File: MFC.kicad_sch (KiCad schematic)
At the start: 29 parts, among them J1 DA15_Receptacle_MountingHoles, J12 Conn_01x01_Pin, J2 Conn_01x04_Pin, J4 647676-3, J5 Conn_01x03_Pin, J6 Conn_01x03_Pin, J7 Conn_01x02_Pin, J8 Conn_01x03_Socket

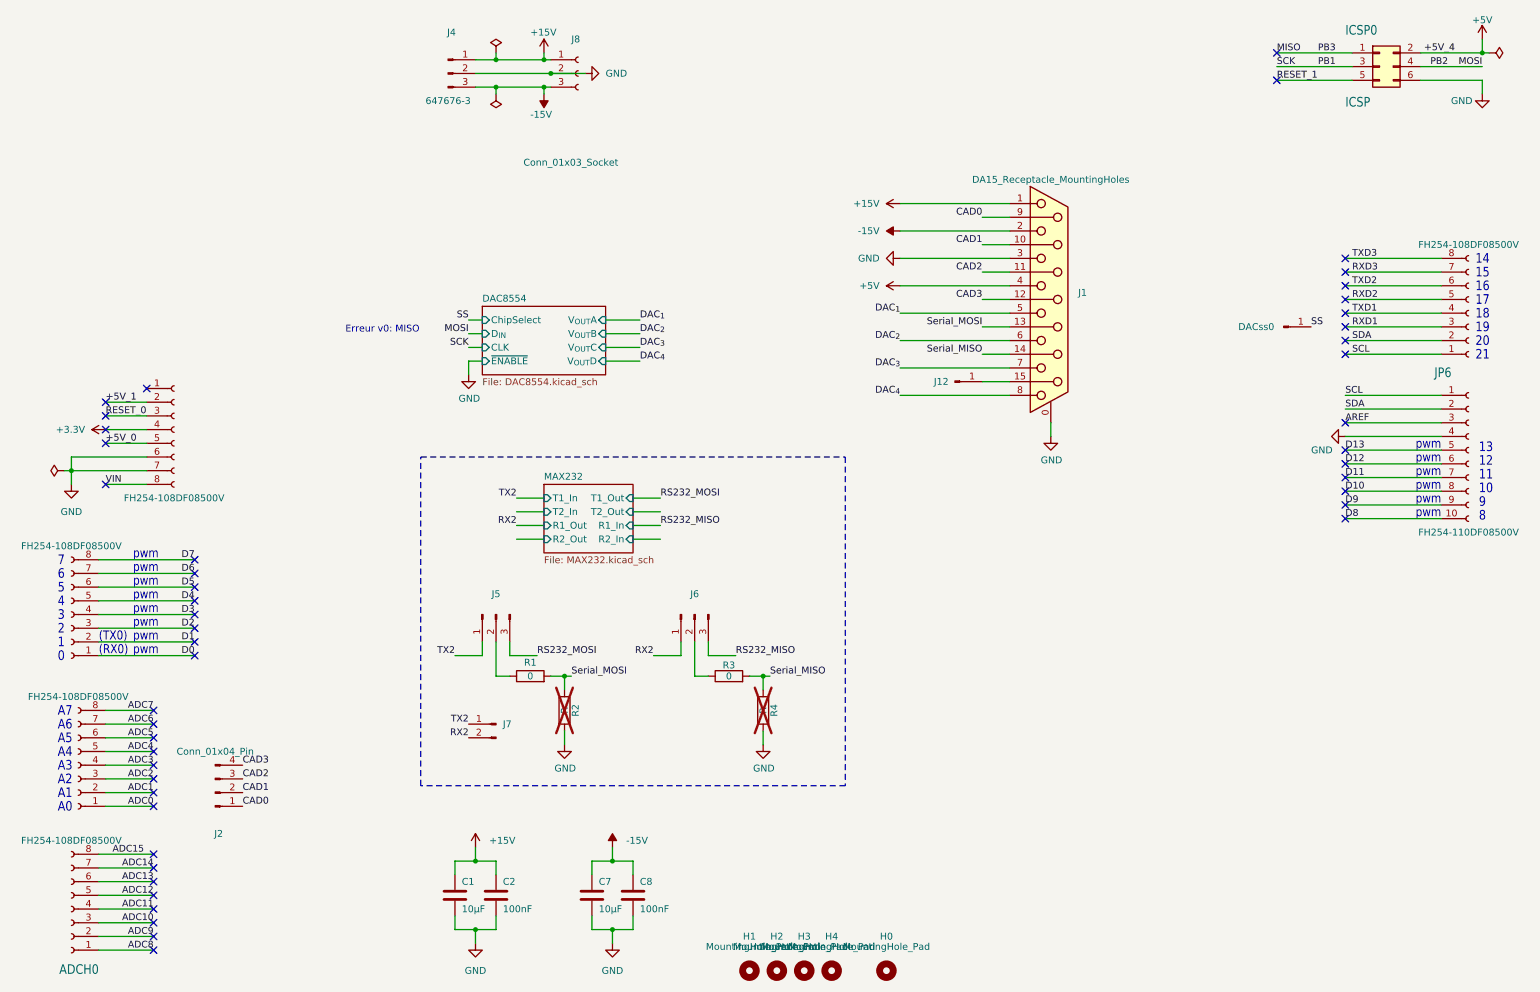
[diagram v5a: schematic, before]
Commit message: Updated to kicad 9
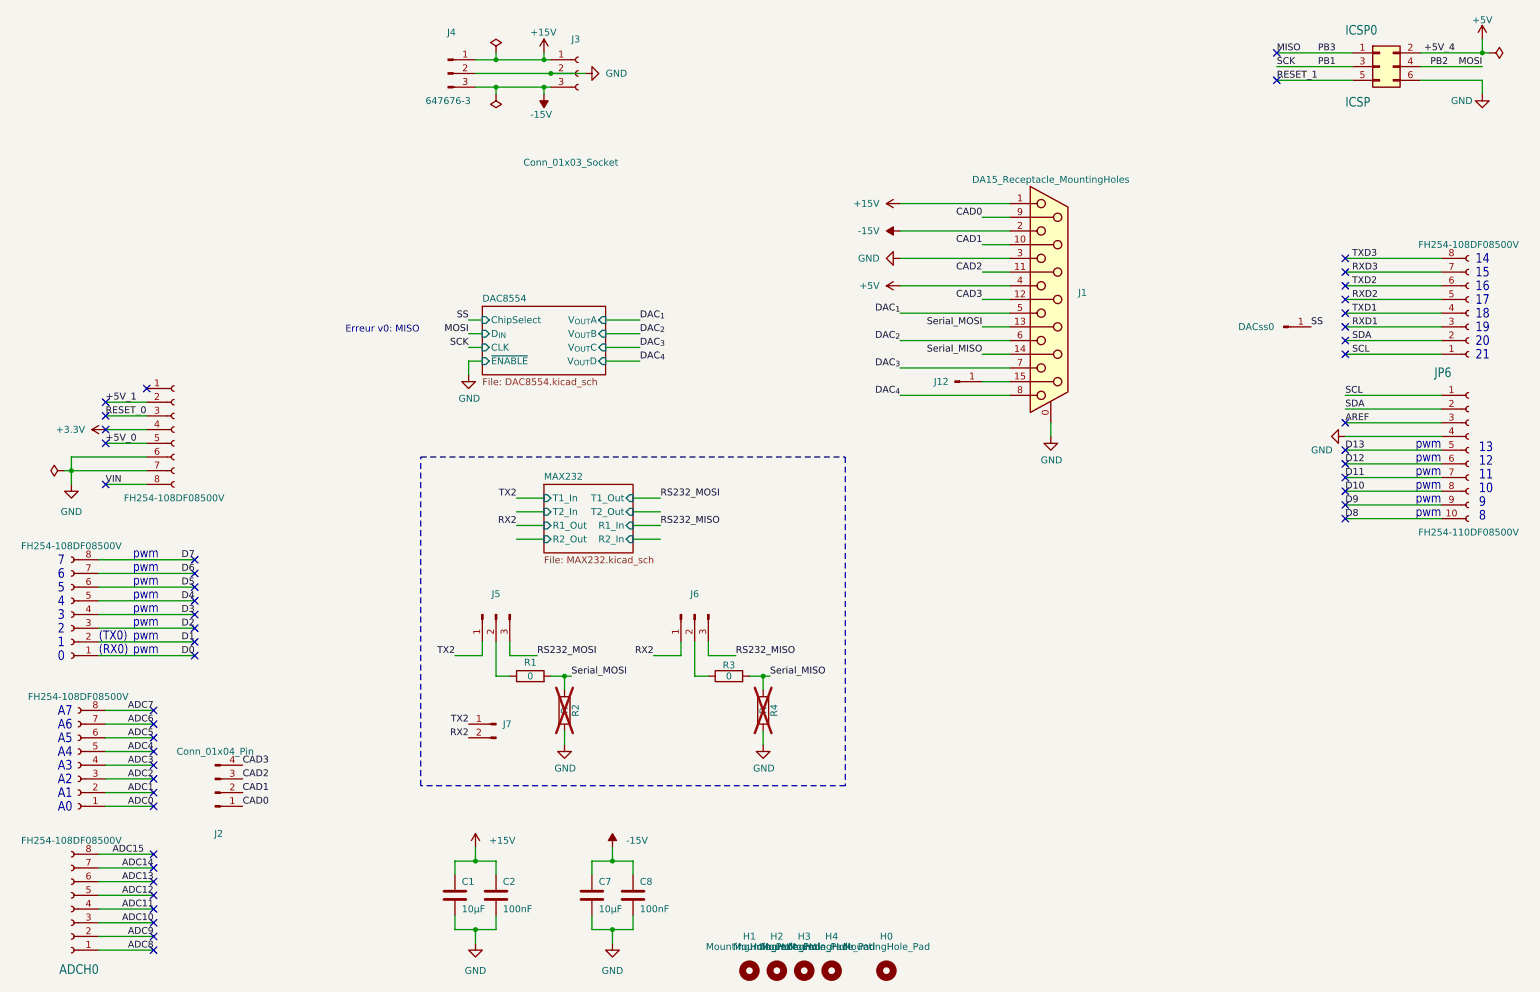
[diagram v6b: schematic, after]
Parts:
- renumbered J8 to J3
